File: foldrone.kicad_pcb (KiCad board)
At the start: 2 copper layers, 48 parts, among them IC1 ATMEGA328P-M, Q1 STS5NF60L, Q2 STS5NF60L, Q3 STS5NF60L, Q4 STS5NF60L, SW1 Reset, SW2 LimitSW, U1 3.3_lod, U2 TLV1117-33IDCY, U3 MPU-6050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

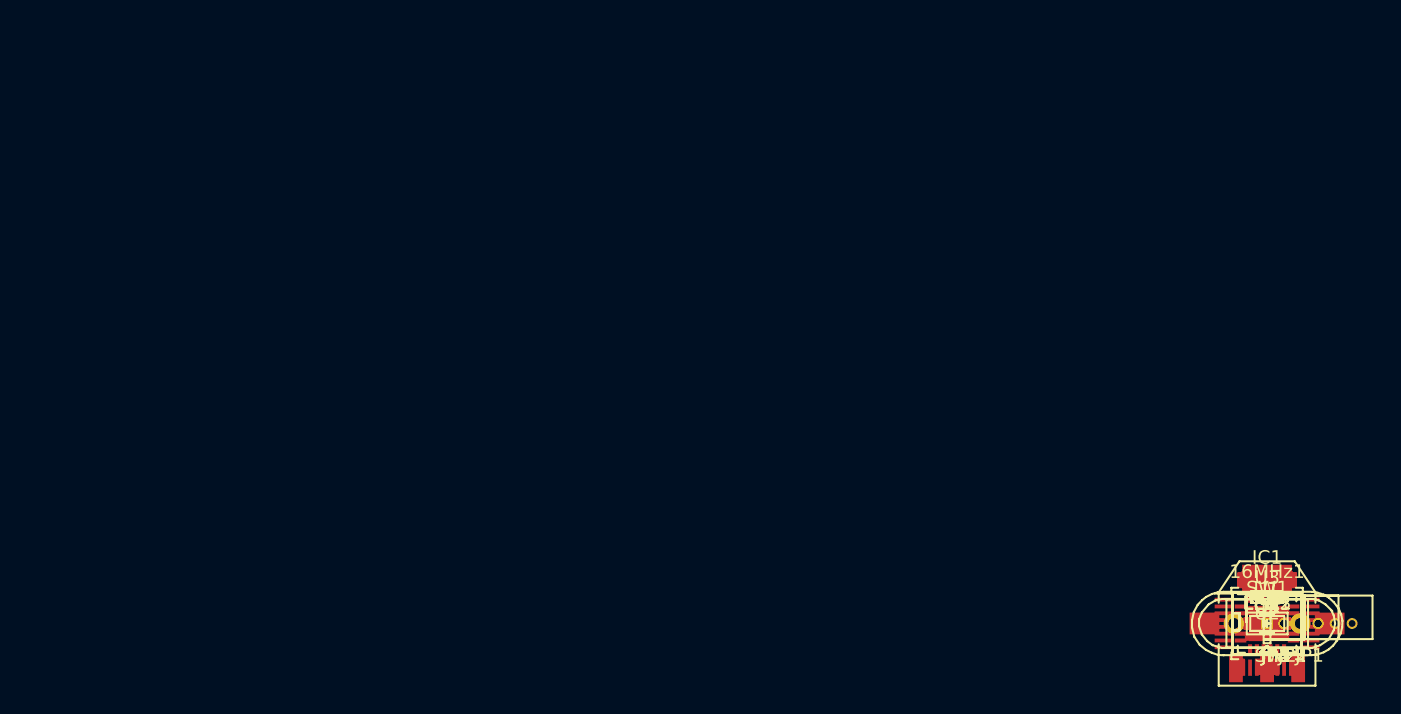
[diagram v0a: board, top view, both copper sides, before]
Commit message: Proto PCB ready
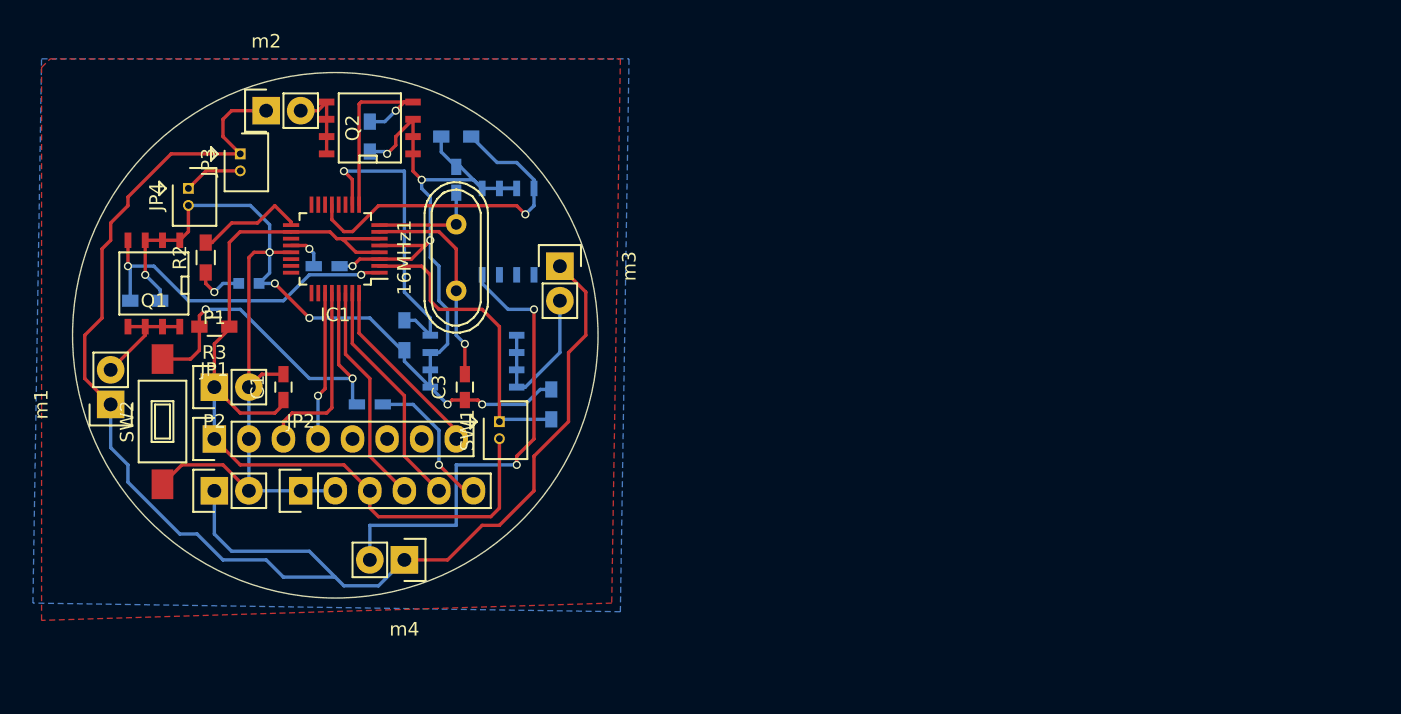
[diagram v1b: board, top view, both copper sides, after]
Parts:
- removed C10: 10μF, Capacitors_SMD:C_0603_HandSoldering
- removed C11: 0.01μF, Capacitors_SMD:C_0603_HandSoldering
- removed C12, C13, C14, C6, C7: 0.1μF, Capacitors_SMD:C_0603_HandSoldering
- removed C8: 4.7μF, Capacitors_SMD:C_0603_HandSoldering
- removed C9: 2200pF, Capacitors_SMD:C_0603_HandSoldering
- removed LED2: Green, LEDs:LED_0603
- removed LED3: Red, LEDs:LED_0603
- removed R10, R11, R12: 4.7K, Resistors_SMD:R_0603_HandSoldering
- removed R8, R9: 10K, Resistors_SMD:R_0603_HandSoldering
- removed U1: 3.3_lod, TO_SOT_Packages_SMD:SOT-23-5
- removed U2: TLV1117-33IDCY, TO_SOT_Packages_SMD:SOT-223
- removed U3: MPU-6050, Housings_DFN_QFN:QFN-24-1EP_4x4mm_Pitch0.5mm
- added P1: Vout01, Socket_Strips:Socket_Strip_Straight_1x02, F.Cu at (71.1, 87.6)
- added P2: CONN_01X02, Socket_Strips:Socket_Strip_Straight_1x02, F.Cu at (71.1, 95.2)
- C1: value 10μF -> 0.1μF
- C2: value 1μF -> 0.1μF; moved to B.Cu
- C3: value 0.1μF -> 22pF
- C4, Q3, Q4, R1, R5, R6, R7: moved to B.Cu
- C5: value 22pF -> 0.1μF; moved to B.Cu
- JP1: value CONN_01X06 -> CONN_01X08; footprint Connectors_Molex:Molex_PicoBlade_53047-0610 -> Socket_Strips:Socket_Strip_Straight_1x08
- JP2: value CONN_01X04 -> CONN_01X06; footprint Connectors_Molex:Molex_PicoBlade_53047-0410 -> Socket_Strips:Socket_Strip_Straight_1x06
- LED1: value Red -> Green; moved to B.Cu
- R2: value 10K -> 330
- R4: value 330 -> 10K; moved to B.Cu
- SW1: value Reset -> LimitSW; footprint Buttons_Switches_SMD:SW_SPST_FSMSM -> Connectors_Molex:Molex_PicoBlade_53047-0210
- SW2: value LimitSW -> Reset; footprint Connectors_Molex:Molex_PicoBlade_53047-0210 -> Buttons_Switches_SMD:SW_SPST_FSMSM
- m1, m2, m3, m4: footprint Connectors_Molex:Molex_PicoBlade_53047-0210 -> Socket_Strips:Socket_Strip_Straight_1x02
- moved m1 86.5 mm to (63.5, 88.9), turned to 90 degrees
- moved R4 85.8 mm to (66.0, 81.3), turned to 180 degrees
- moved Q1 85.6 mm to (66.7, 80.0), turned to 180 degrees
- moved JP4 85.5 mm to (69.2, 73.0), turned to 270 degrees
- moved JP3 83.0 mm to (73.0, 70.5), turned to 270 degrees
- moved m2 82.7 mm to (74.9, 67.3)
- moved SW2 82.5 mm to (67.3, 90.2), turned to 90 degrees
- moved R2 82.5 mm to (70.5, 78.1), turned to 90 degrees
- moved R3 80.4 mm to (71.1, 83.2), turned to 180 degrees
- moved LED1 78.9 mm to (73.7, 80.0), turned to 180 degrees
- moved JP1 78.6 mm to (71.1, 91.4)
- moved Q2 75.3 mm to (82.5, 68.6), turned to 90 degrees
- moved R5 75.0 mm to (82.5, 69.2), turned to 90 degrees
- moved C1 74.4 mm to (76.2, 87.6), turned to 90 degrees
- moved C2 73.9 mm to (79.4, 78.7)
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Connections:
- C1 pad 1: RAW -> VCC
- C2 pad 1: VCC -> Net-(C2-Pad1)
- C3 pad 1: DTR -> GND
- C3 pad 2: Net-(C3-Pad2) -> Net-(16MHz1-Pad1)
- C4 pad 2: Net-(16MHz1-Pad1) -> Net-(16MHz1-Pad2)
- C5 pad 1: GND -> DTR
- C5 pad 2: Net-(16MHz1-Pad2) -> Net-(C5-Pad2)
- IC1 pad 20: Net-(C6-Pad1) -> Net-(C2-Pad1)
- IC1 pad 29: Net-(C3-Pad2) -> Net-(C5-Pad2)
- JP1 pad 1: GND -> VCC
- JP1 pad 3: VCC -> SCL
- JP1 pad 4: RXD -> SDA
- JP1 pad 5: TXD -> Net-(JP1-Pad5)
- JP1 pad 6: DTR -> Net-(JP1-Pad6)
- JP2 pad 1: TXD -> GND
- JP2 pad 2: RXD -> GND
- JP2 pad 3: GND -> VCC
- JP2 pad 4: VCC -> RXD
- LED1 pad 1: Net-(LED1-Pad1) -> GND
- LED1 pad 2: VCC -> Net-(LED1-Pad2)
- R1 pad 1: Net-(LED1-Pad1) -> FoldSW
- R2 pad 1: VCC -> Net-(LED1-Pad2)
- R2 pad 2: Net-(C3-Pad2) -> Net-(IC1-Pad17)
- R3 pad 1: FoldSW -> VCC
- R3 pad 2: GND -> Net-(C5-Pad2)
- R4 pad 1: Net-(LED2-Pad2) -> GND
- R4 pad 2: Net-(IC1-Pad17) -> PWM01
- R5 pad 2: PWM01 -> PWM02
- R6 pad 2: PWM02 -> PWM03
- R7 pad 2: PWM03 -> PWM04
- SW1 pad 1: GND -> FoldSW
- SW1 pad 2: Net-(C3-Pad2) -> VCC
- SW2 pad 1: FoldSW -> GND
- SW2 pad 2: VCC -> Net-(C5-Pad2)
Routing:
- net GND: track 0.00 -> 137.9 mm, vias 0 -> 10
- net RAW: track 0.00 -> 107.8 mm
- net VCC: track 0.00 -> 65.8 mm
- net Net-(Q4-Pad5): track 0.00 -> 35.0 mm, vias 0 -> 2
- net Net-(C5-Pad2): track 0.00 -> 27.8 mm, vias 0 -> 2
- net PWM04: track 0.00 -> 25.5 mm, vias 0 -> 1
- net PWM01: track 0.00 -> 24.9 mm, vias 0 -> 2
- net FoldSW: track 0.00 -> 22.8 mm
- net PWM03: track 0.00 -> 22.4 mm, vias 0 -> 1
- net TXD: track 0.00 -> 17.2 mm
- net RXD: track 0.00 -> 16.3 mm
- net Net-(16MHz1-Pad1): track 0.00 -> 15.8 mm, vias 0 -> 1
- net PWM02: track 0.00 -> 15.2 mm, vias 0 -> 1
- net SCL: track 0.00 -> 13.7 mm
- net INT: track 0.00 -> 13.7 mm
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- added copper zone on B.Cu, net GND
- added copper zone on F.Cu, net GND
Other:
- board outline added: 38.6 x 38.6 mm
